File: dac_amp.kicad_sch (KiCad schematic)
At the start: 21 parts, among them U11 Opamp_Dual

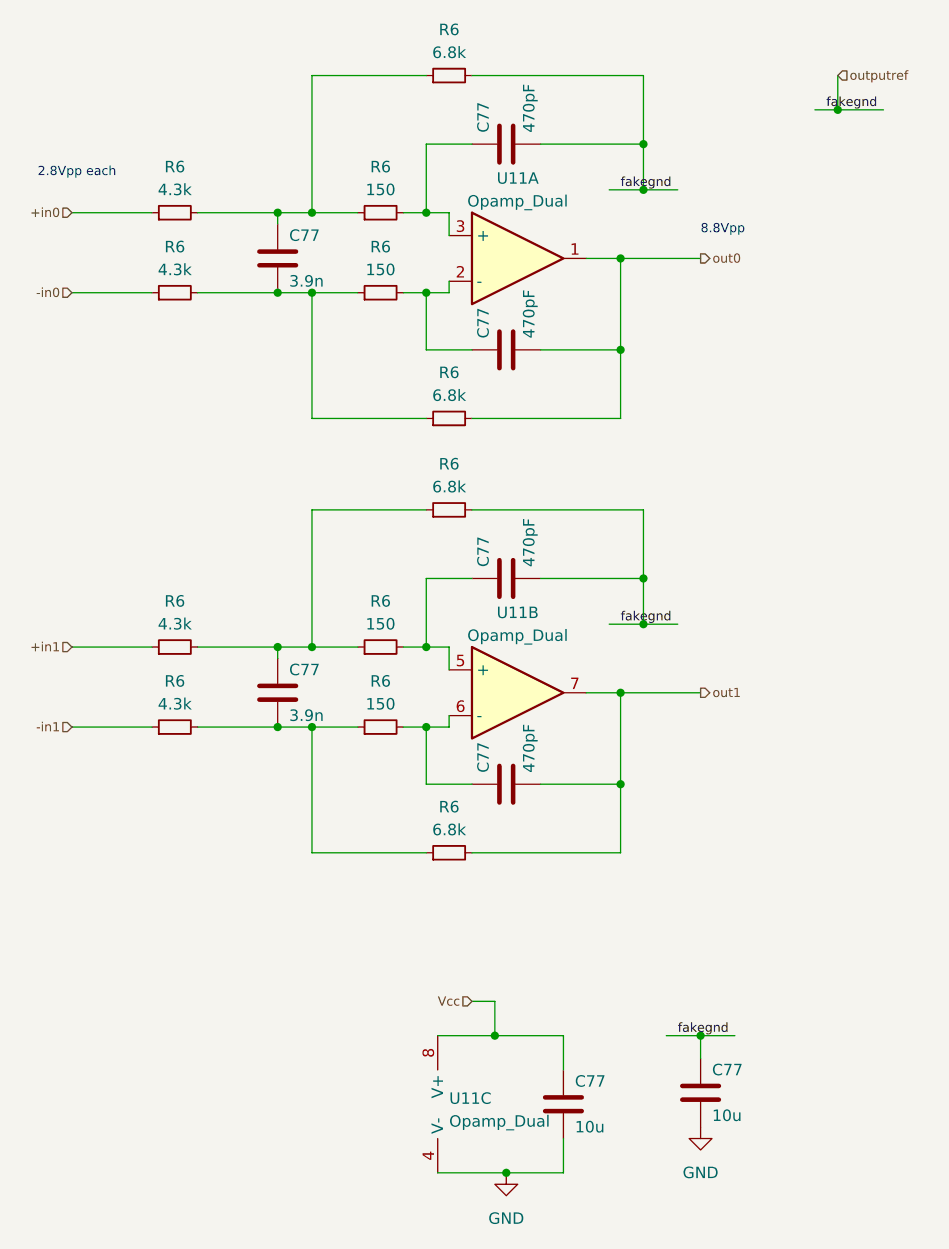
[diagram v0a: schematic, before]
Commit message: update to kicad 8
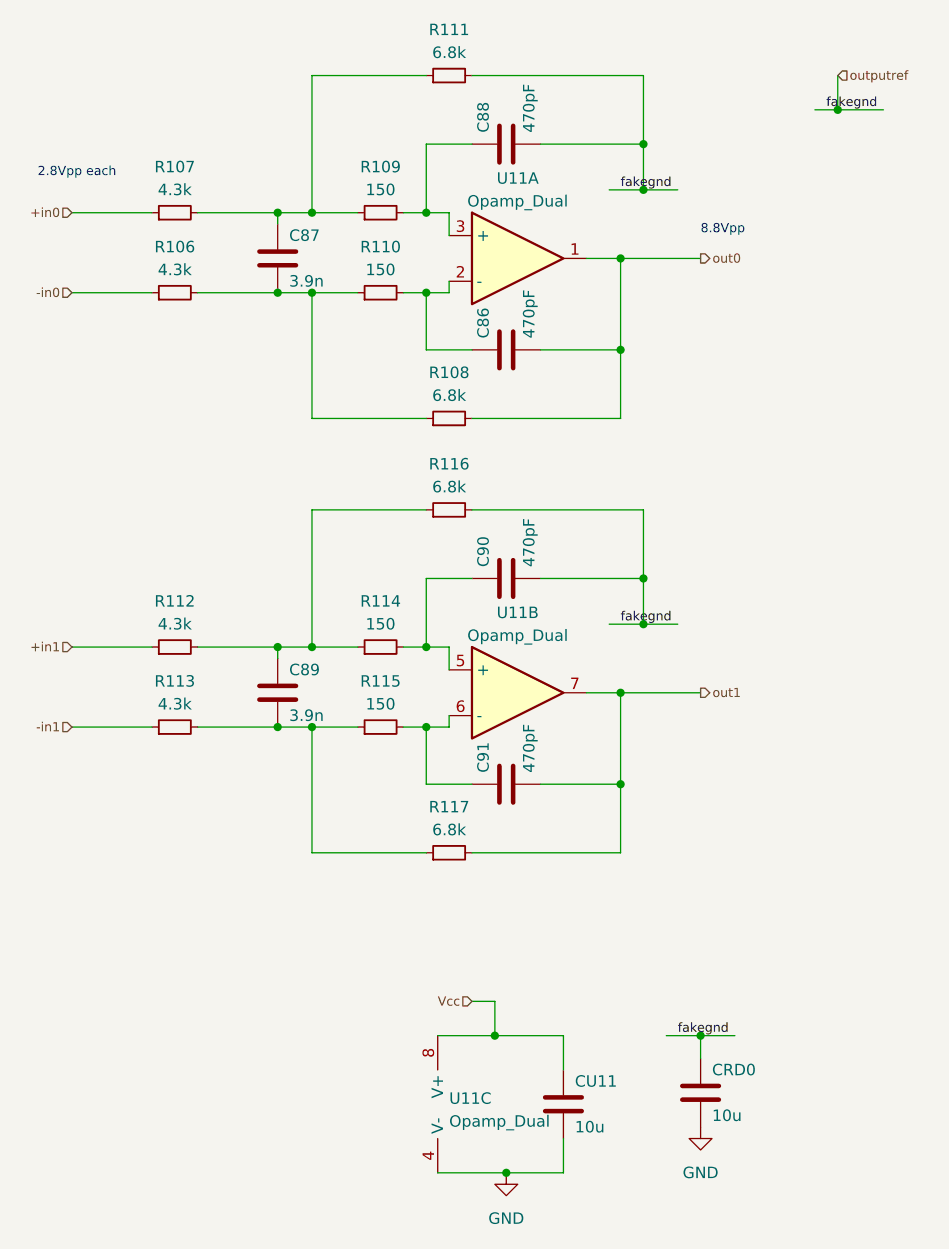
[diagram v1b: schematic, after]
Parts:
- renumbered C77 to C86, C77 to C87, C77 to C88, C77 to C89, C77 to C90, C77 to C91, C77 to CRD0, C77 to CU11, R6 to R106, R6 to R107, R6 to R108, R6 to R109, R6 to R110, R6 to R111, R6 to R112, R6 to R113, R6 to R114, R6 to R115, R6 to R116, R6 to R117

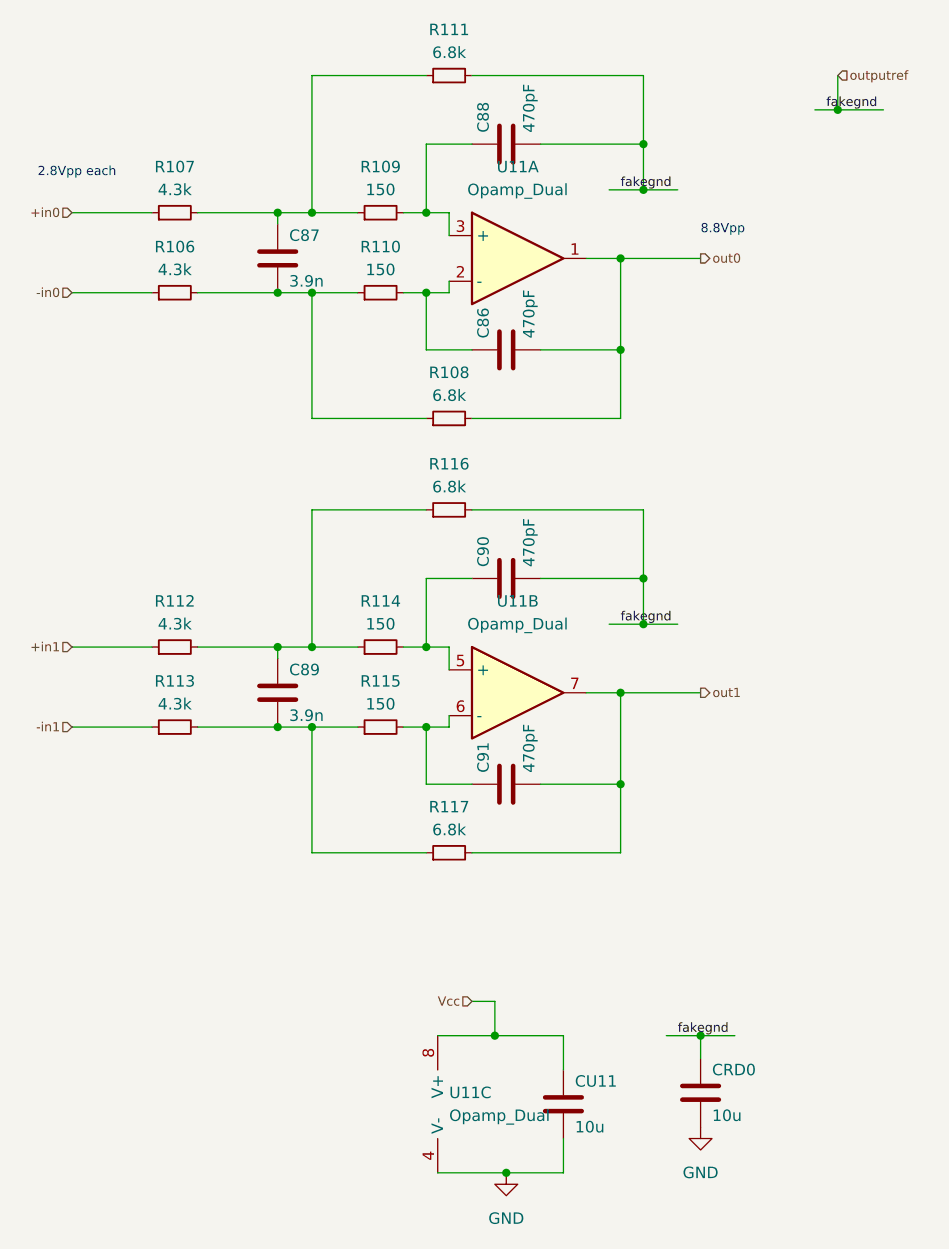
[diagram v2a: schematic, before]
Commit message: add power input +...
+ tons of fixes, footprint assignments, etc
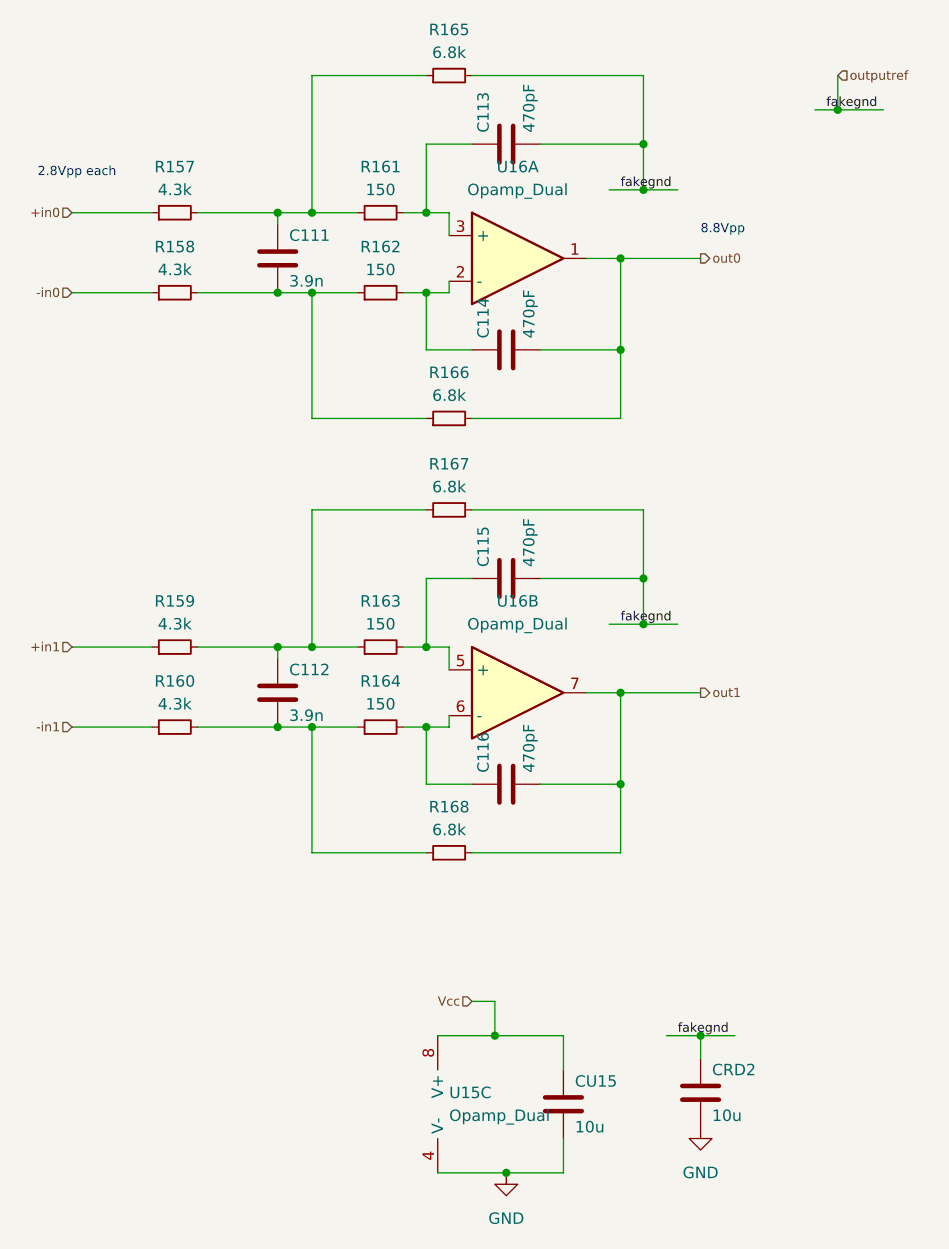
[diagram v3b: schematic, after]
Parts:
- C111: renamed from C87; footprint (none) -> invendelirium_audio:C_0603
- C112: renamed from C89; footprint (none) -> invendelirium_audio:C_0603
- U15, U16: renamed from U11; footprint (none) -> invendelirium_audio:SOIC-8; PN (none) -> NE5532DRG4
- renumbered C88 to C113, C86 to C114, C90 to C115, C91 to C116, CRD0 to CRD2, CU11 to CU15, R107 to R157, R106 to R158, R112 to R159, R113 to R160, R109 to R161, R110 to R162, R114 to R163, R115 to R164, R111 to R165, R108 to R166, R116 to R167, R117 to R168

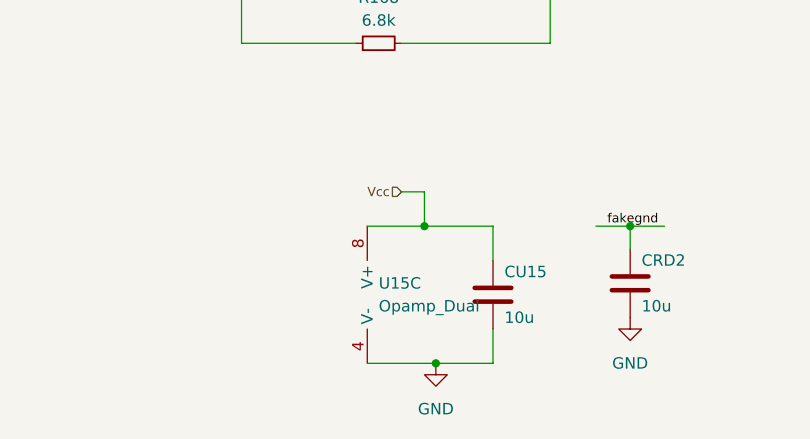
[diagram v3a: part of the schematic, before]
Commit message: fix gate association U15 U16
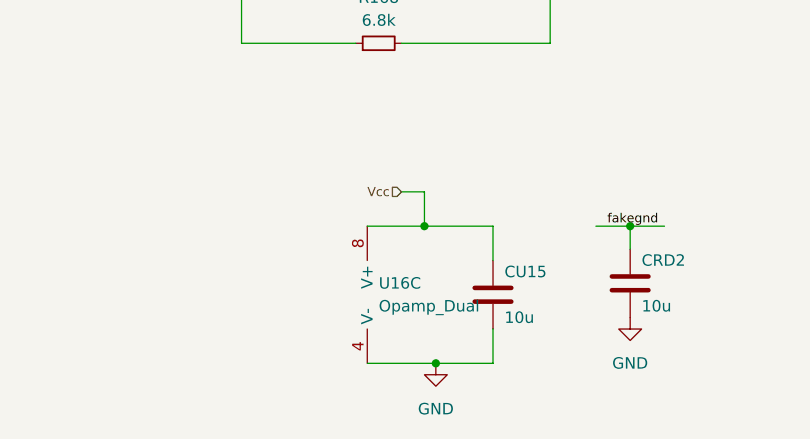
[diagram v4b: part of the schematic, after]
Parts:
- renumbered U15 to U16
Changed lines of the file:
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@@
 		(dnp no)
 		(fields_autoplaced yes)
-		(property "Reference" "U15"
+		(property "Reference" "U16"
 			(at 60.96 133.3499 0)
 			(effects
@@
 			(project ""
 				(path "/310059c1-d84b-43e2-9c9a-0e426c534a12/7069641c-0ed4-4995-a63e-1f44999c4edd/906b57e9-9db9-476e-b6b6-ee649f34d32d"
-					(reference "U15")
+					(reference "U16")
 					(unit 3)
 				)

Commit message: fill in some part numbers
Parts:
- C111, C112: PN (none) -> GCM1885C1H392GA16D
- C113, C114, C115, C116: PN (none) -> VJ0603A471GXXCW1BC
- R157, R158, R159, R160: PN (none) -> RT0603DRE074K32L
- R161, R162, R163, R164: PN (none) -> RT0603DRD07150RL
- R165, R166, R167, R168: PN (none) -> RT0603DRE076K8L
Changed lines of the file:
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@@
+			)
+		)
+		(property "PN" "VJ0603A471GXXCW1BC"
+			(at 67.31 76.2 0)
+			(effects
+				(font
+					(size 1.27 1.27)
+				)
+				(hide yes)
 			)
 		)
@@
 			)
 		)
+		(property "PN" "RT0603DRD07150RL"
+			(at 53.34 44.45 0)
+			(effects
+				(font
+					(size 1.27 1.27)
+				)
+				(hide yes)
+			)
+		)
 		(pin "1"
 		)
@@
 			)
 		)
+		(property "PN" "RT0603DRE074K32L"
+			(at 30.48 35.56 0)
+			(effects
+				(font
+					(size 1.27 1.27)
+				)
+				(hide yes)
+			)
+		)
 		(pin "1"
 		)
@@
 			)
 		)
+		(property "PN" "VJ0603A471GXXCW1BC"
+			(at 67.31 99.06 0)
+			(effects
+				(font
+					(size 1.27 1.27)
+				)
+				(hide yes)
+			)
+		)
 		(pin "1"
 		)
@@
 				(font
 					(size 1.27 1.27)
+				)
+				(hide yes)
+			)
+		)
+		(property "PN" "GCM1885C1H392GA16D"
+			(at 41.91 88.9 0)
+			(effects
+				(font
+					(size 1.016 1.016)
 				)
 				(hide yes)
@@
 			)
 		)
+		(property "PN" "RT0603DRD07150RL"
+			(at 53.34 83.82 0)
+			(effects
+				(font
+					(size 1.27 1.27)
+				)
+				(hide yes)
+			)
+		)
 		(pin "1"
 		)
@@
 			)
 		)
+		(property "PN" "RT0603DRD07150RL"
+			(at 53.34 35.56 0)
+			(effects
+				(font
+					(size 1.27 1.27)
+				)
+				(hide yes)
+			)
+		)
 		(pin "1"
 		)
@@
 			)
 		)
+		(property "PN" "VJ0603A471GXXCW1BC"
+			(at 67.31 50.8 0)
+			(effects
+				(font
+					(size 1.27 1.27)
+				)
+				(hide yes)
+			)
+		)
 		(pin "1"
 		)
@@
 				(font
 					(size 1.27 1.27)
+				)
+				(hide yes)
+			)
+		)
+		(property "PN" "VJ0603A471GXXCW1BC"
+			(at 67.31 27.94 0)
+			(effects
+				(font
+					(size 1.016 1.016)
 				)
 				(hide yes)
@@
 			)
 		)
+		(property "PN" "RT0603DRE076K8L"
+			(at 60.96 58.42 0)
+			(effects
+				(font
+					(size 1.27 1.27)
+				)
+				(hide yes)
+			)
+		)
 		(pin "1"
 		)
@@
 			)
 		)
+		(property "PN" "RT0603DRE076K8L"
+			(at 60.96 106.68 0)
+			(effects
+				(font
+					(size 1.27 1.27)
+				)
+				(hide yes)
+			)
+		)
 		(pin "1"
 		)
@@
 			)
 		)
+		(property "PN" "RT0603DRE074K32L"
+			(at 30.48 83.82 0)
+			(effects
+				(font
+					(size 1.27 1.27)
+				)
+				(hide yes)
+			)
+		)
 		(pin "1"
 		)
@@
 			)
 		)
+		(property "PN" "RT0603DRE074K32L"
+			(at 30.48 44.45 0)
+			(effects
+				(font
+					(size 1.27 1.27)
+				)
+				(hide yes)
+			)
+		)
 		(pin "1"
 		)
@@
 			)
 		)
+		(property "PN" "RT0603DRE074K32L"
+			(at 30.48 92.71 0)
+			(effects
+				(font
+					(size 1.27 1.27)
+				)
+				(hide yes)
+			)
+		)
 		(pin "1"
 		)
@@
 			)
 		)
+		(property "PN" "RT0603DRE076K8L"
+			(at 60.96 20.32 0)
+			(effects
+				(font
+					(size 1.27 1.27)
+				)
+				(hide yes)
+			)
+		)
 		(pin "1"
 		)
@@
 			)
 		)
+		(property "PN" "RT0603DRD07150RL"
+			(at 53.34 92.71 0)
+			(effects
+				(font
+					(size 1.27 1.27)
+				)
+				(hide yes)
+			)
+		)
 		(pin "1"
 		)
@@
 			)
 		)
+		(property "PN" "RT0603DRE076K8L"
+			(at 60.96 68.58 0)
+			(effects
+				(font
+					(size 1.27 1.27)
+				)
+				(hide yes)
+			)
+		)
 		(pin "1"
 		)
@@
 				)
 				(hide yes)
+			)
+		)
+		(property "PN" "GCM1885C1H392GA16D"
+			(at 41.91 40.64 0)
+			(effects
+				(font
+					(size 1.016 1.016)
+				)
+				(hide yes)

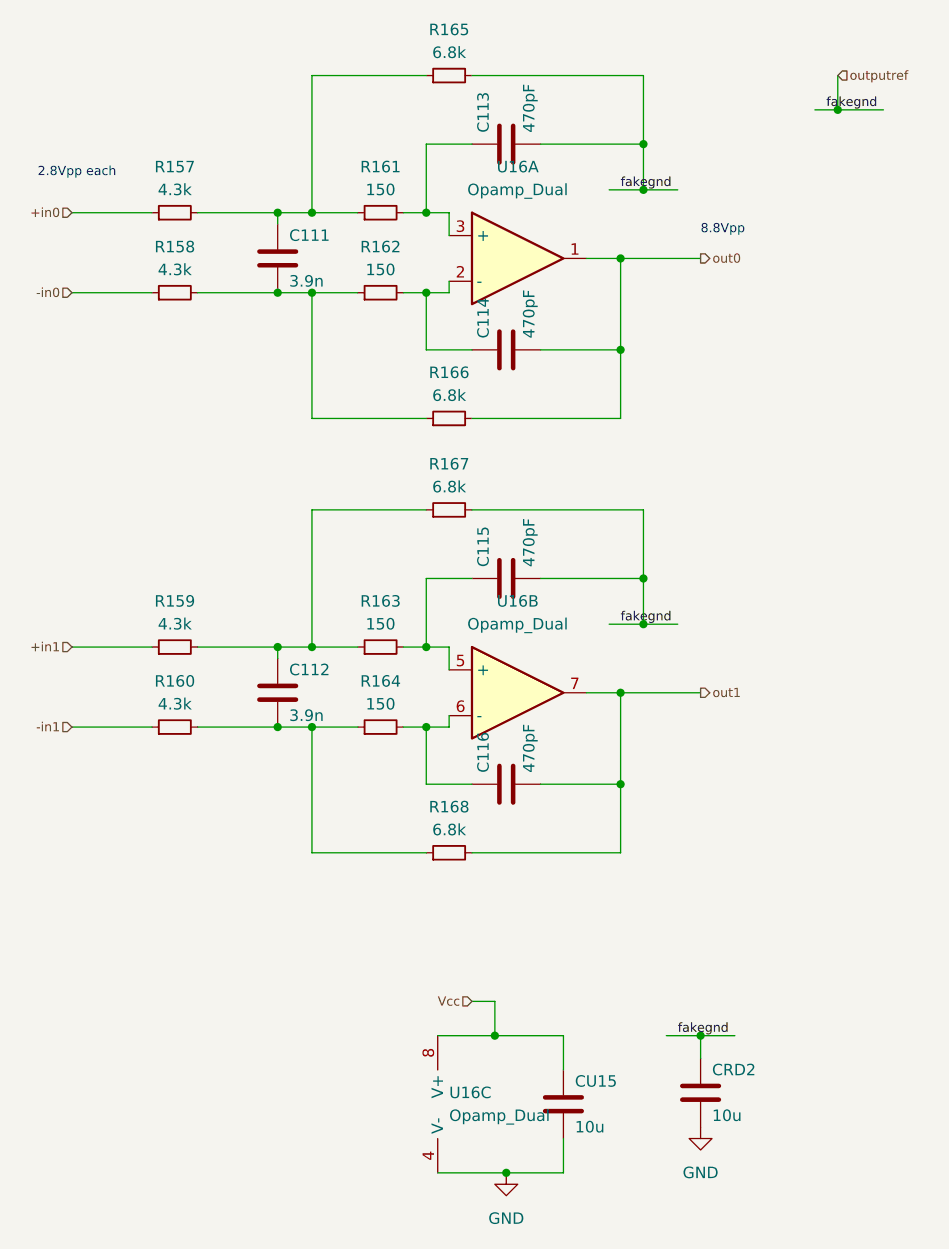
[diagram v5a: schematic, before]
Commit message: update partnumbers to what was bought
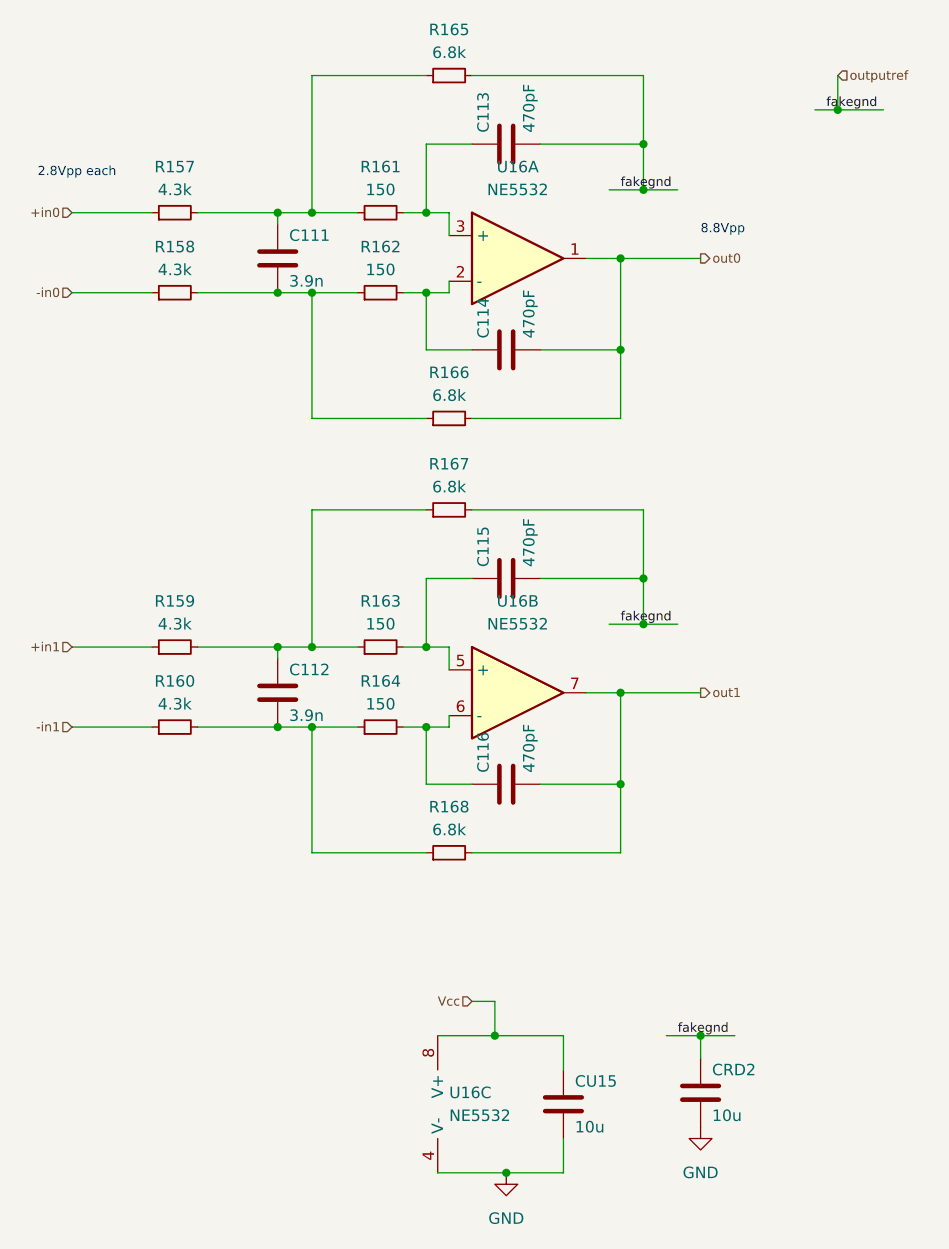
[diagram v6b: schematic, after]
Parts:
- U16: value Opamp_Dual -> NE5532; PN NE5532DRG4 -> NE5532DR
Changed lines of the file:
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@@
 			)
 		)
-		(property "Value" "Opamp_Dual"
+		(property "Value" "NE5532"
 			(at 68.58 33.02 0)
 			(effects
@@
 			)
 		)
-		(property "PN" "NE5532DRG4"
+		(property "PN" "NE5532DR"
 			(at 68.58 40.64 0)
 			(effects
@@
 			)
 		)
-		(property "Value" "Opamp_Dual"
+		(property "Value" "NE5532"
 			(at 60.96 135.8899 0)
 			(effects
@@
 			)
 		)
-		(property "PN" "NE5532DRG4"
+		(property "PN" "NE5532DR"
 			(at 62.23 134.62 0)
 			(effects
@@
 			)
 		)
-		(property "Value" "Opamp_Dual"
+		(property "Value" "NE5532"
 			(at 68.58 81.28 0)
 			(effects
@@
 			)
 		)
-		(property "PN" "NE5532DRG4"
+		(property "PN" "NE5532DR"
 			(at 68.58 88.9 0)
 			(effects
